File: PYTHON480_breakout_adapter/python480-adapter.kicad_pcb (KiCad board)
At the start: 2 copper layers, 19.1 x 44.5 mm, 3 parts, among them J1 Conn_02x12_Odd_Even, J2 Conn_02x05_Odd_Even, J3 Hirose_DF12_DF12E3.0-30DP

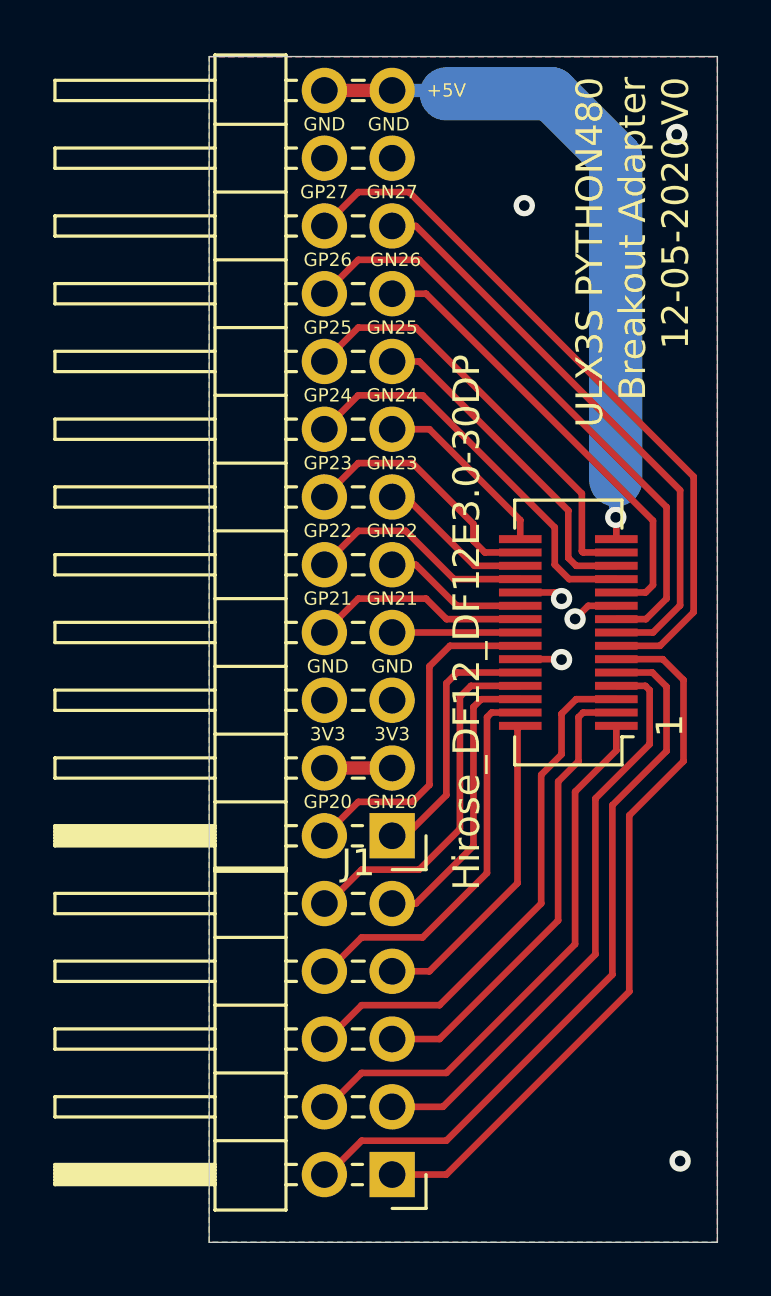
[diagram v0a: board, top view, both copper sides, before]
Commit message: re-label all pins
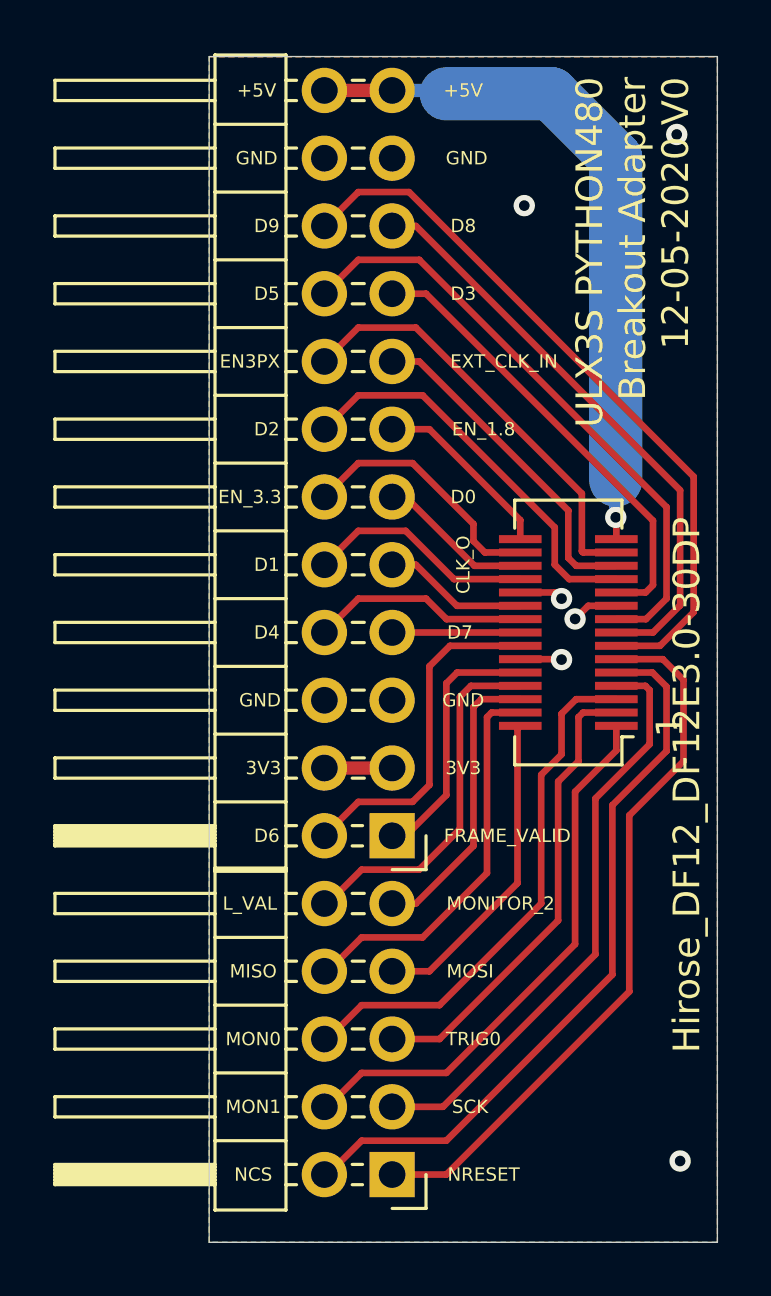
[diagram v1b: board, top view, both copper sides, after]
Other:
- board text added: "CLK_O"
- board text added: "D0"
- board text added: "D1"
- board text added: "D2"
- board text added: "D3"
- board text added: "D4"
- board text added: "D5"
- board text added: "D6"
- board text added: "D7"
- board text added: "D8"
- board text added: "D9"
- board text added: "EN3PX"
- board text added: "EN_1.8"
- board text added: "EN_3.3"
- board text added: "EXT_CLK_IN"
- board text added: "FRAME_VALID"
- board text added: "L_VAL"
- board text added: "MISO"
- board text added: "MON0"
- board text added: "MON1"
- board text added: "MONITOR_2"
- board text added: "MOSI"
- board text added: "NCS"
- board text added: "NRESET"
- board text added: "SCK"
- board text added: "TRIG0"
- board text removed: "GN15"
- board text removed: "GN16"
- board text removed: "GN17"
- board text removed: "GN18"
- board text removed: "GN19"
- board text removed: "GN20"
- board text removed: "GN21"
- board text removed: "GN22"
- board text removed: "GN23"
- board text removed: "GN24"
- board text removed: "GN25"
- board text removed: "GN26"
- board text removed: "GN27"
- board text removed: "GP15"
- board text removed: "GP16"
- board text removed: "GP17"
- board text removed: "GP18"
- board text removed: "GP19"
- board text removed: "GP20"
- board text removed: "GP21"
- board text removed: "GP22"
- board text removed: "GP23"
- board text removed: "GP24"
- board text removed: "GP25"
- board text removed: "GP26"
- board text removed: "GP27"
